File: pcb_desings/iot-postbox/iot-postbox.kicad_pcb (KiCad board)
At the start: 2 copper layers, 31 x 43.6 mm, 39 parts, among them J1 Switch_1, J2 Switch_2, J3 PowerIn, J4 USB_B_Micro, J5 Battery, J6 Battery, SW1 POWER, U1 ESP-12F, U2 TTL_UART_adapter_iot_postbox, U3 TP4056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

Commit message: Updated iot-postbox sch and pcb to v0.2 correcting Switch references
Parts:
- J1: renamed from J2; value Switch_2 -> Switch_1
- J2: renamed from J1; value Switch_1 -> Switch_2
- R1, R2, R3, R4, R5: value 10k -> 10K
- R11: value 100 -> 100R
- R12: value 100K -> 1M
- R13: value 30K -> 300K
- R6: renamed from R7; value 10k -> 10K
- R7: renamed from R6; value 10k -> 10K
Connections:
- J4 pad 2: (no net) -> Net-(J4-Pad2)
- J4 pad 3: (no net) -> Net-(J4-Pad3)
- J4 pad 4: (no net) -> Net-(J4-Pad4)
- SW1 pad 3: (no net) -> Net-(SW1-Pad3)
- U1 pad 10: (no net) -> Net-(U1-Pad10)
- U1 pad 11: (no net) -> Net-(U1-Pad11)
- U1 pad 12: (no net) -> Net-(U1-Pad12)
- U1 pad 13: (no net) -> Net-(U1-Pad13)
- U1 pad 14: (no net) -> Net-(U1-Pad14)
- U1 pad 4: (no net) -> Net-(U1-Pad4)
- U1 pad 9: (no net) -> Net-(U1-Pad9)
- U3 pad 9: (no net) -> Net-(U3-Pad9)
- U4 pad 4: (no net) -> Net-(U4-Pad4)
- U5 pad 1: (no net) -> Net-(U5-Pad1)
- U5 pad 8: (no net) -> Net-(U5-Pad8)

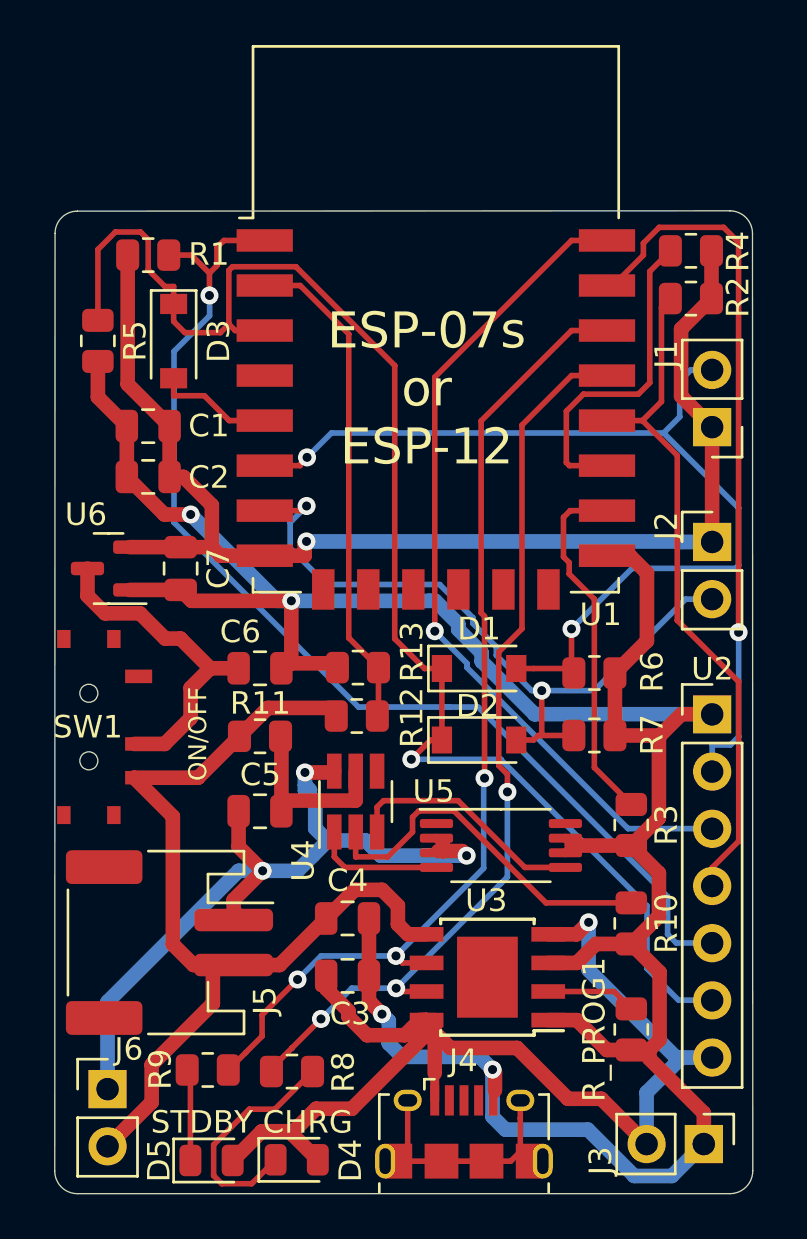
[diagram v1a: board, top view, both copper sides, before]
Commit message: Exported pcb iot-postbox v0.3. Added ws2812b led strip to sch and pcb
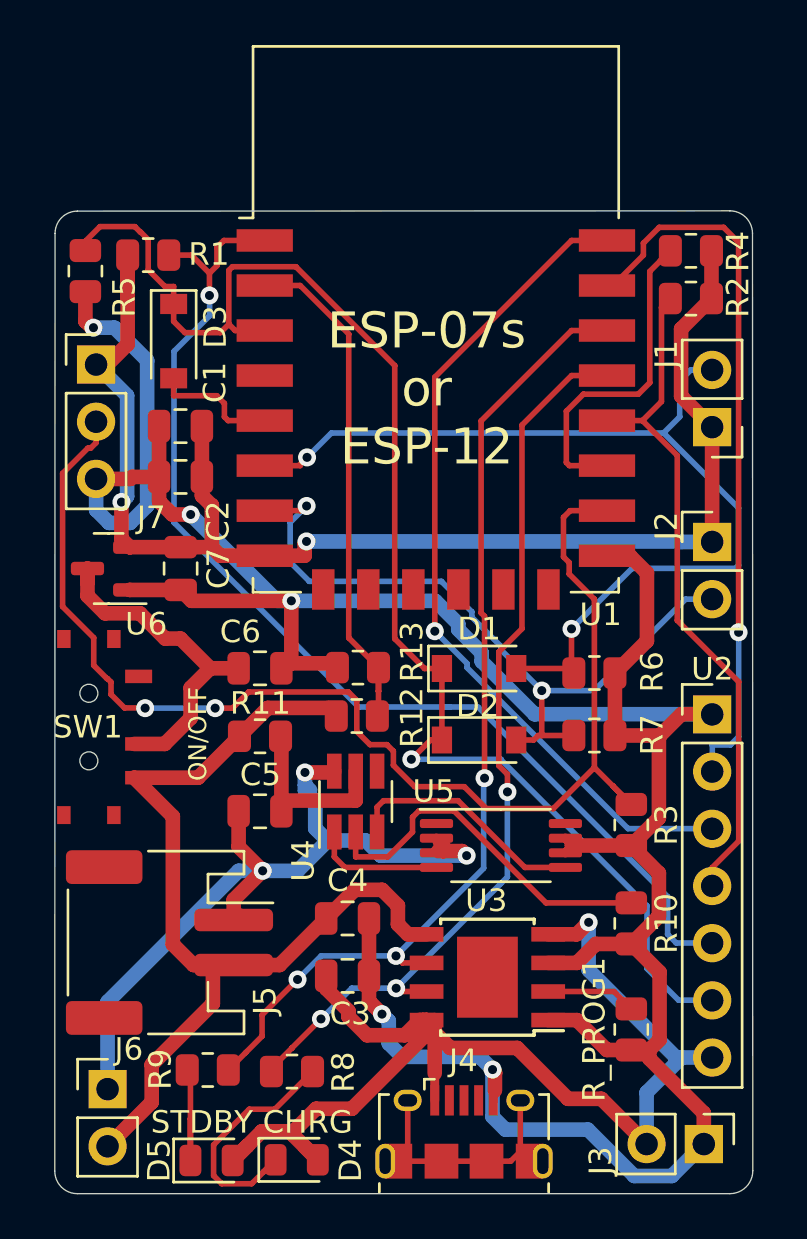
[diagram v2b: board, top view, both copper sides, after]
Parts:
- added J7: LED, Connector_PinHeader_2.54mm:PinHeader_1x03_P2.54mm_Vertical, F.Cu at (101.7, 115.6)
- moved R5 3.15 mm to (101.2, 111.5)
- moved C1 1.43 mm to (105.4, 118.4)
- moved C2 1.43 mm to (105.4, 120.6)
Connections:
- net Net-(R3-Pad1) renamed /GPIO15
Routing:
- net /GPIO15: track 16.1 -> 57.0 mm, vias 0 -> 2
- net IN-: track 122.9 -> 138.7 mm, vias 4 -> 5
- net VCC: track 55.6 -> 63.0 mm, vias 1 -> 2
- net /CH_PD: track 65.5 -> 63.3 mm
- net Net-(D5-Pad1): track 4.08 -> 6.03 mm
- net IN+: track 52.3 -> 54.1 mm
- net /ADC: track 22.2 -> 23.2 mm
- net Net-(D4-Pad1): track 10.4 -> 11.2 mm
- net Net-(R4-Pad1): track 14.6 -> 15.3 mm
- net /OUT: track 14.8 -> 15.4 mm
- net /RX: track 32.0 -> 32.6 mm
- net Net-(R_PROG1-Pad2): track 4.01 -> 4.56 mm
- net /STDBY: track 44.3 -> 44.9 mm
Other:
- board text added: "GND"
- board text added: "GPIO15"
- board text added: "LED"
- board text added: "v0.3"
- board text removed: "v0.2"
